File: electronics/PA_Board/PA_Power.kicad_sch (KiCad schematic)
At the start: 37 parts, among them J5 Conn_01x02, Q1 RD3G01BAT, U4 MP1584, U5 MCP4725, U6 AP2204K-ADJ, U7 TLV70233, U8 INA219AxD

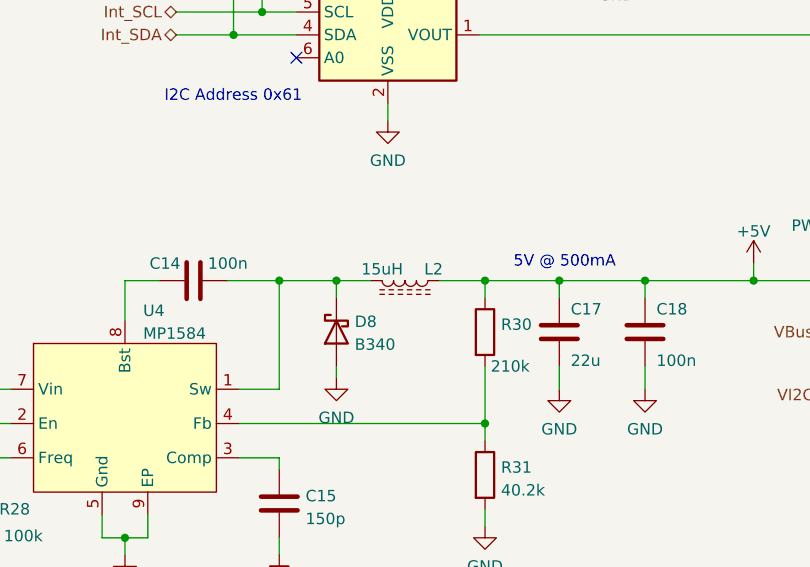
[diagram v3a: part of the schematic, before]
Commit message: Merge branch 'main' of https://github.com/M0LTE/pi-transceiver
Addition of PA Board version 2 Kicad files
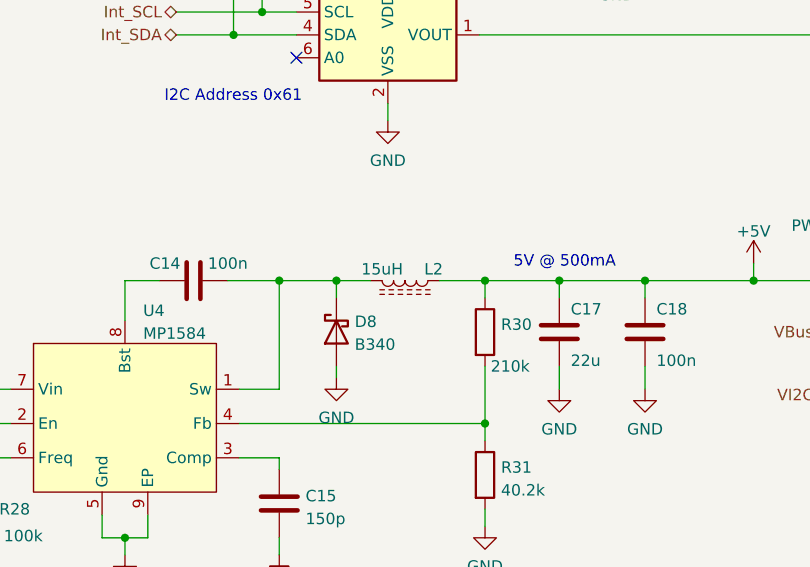
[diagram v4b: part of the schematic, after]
